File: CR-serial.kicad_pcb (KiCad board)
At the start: 2 copper layers, 55.6 x 43.9 mm, 26 parts, among them J1 USB, J2 GPIO, J3 UART0, J4 UART1, J5 UART2, J6 UART3_HV, J7 RS232_0, J8 RS232_1, U1 CP2108-xxx-xM, U2 MAX232

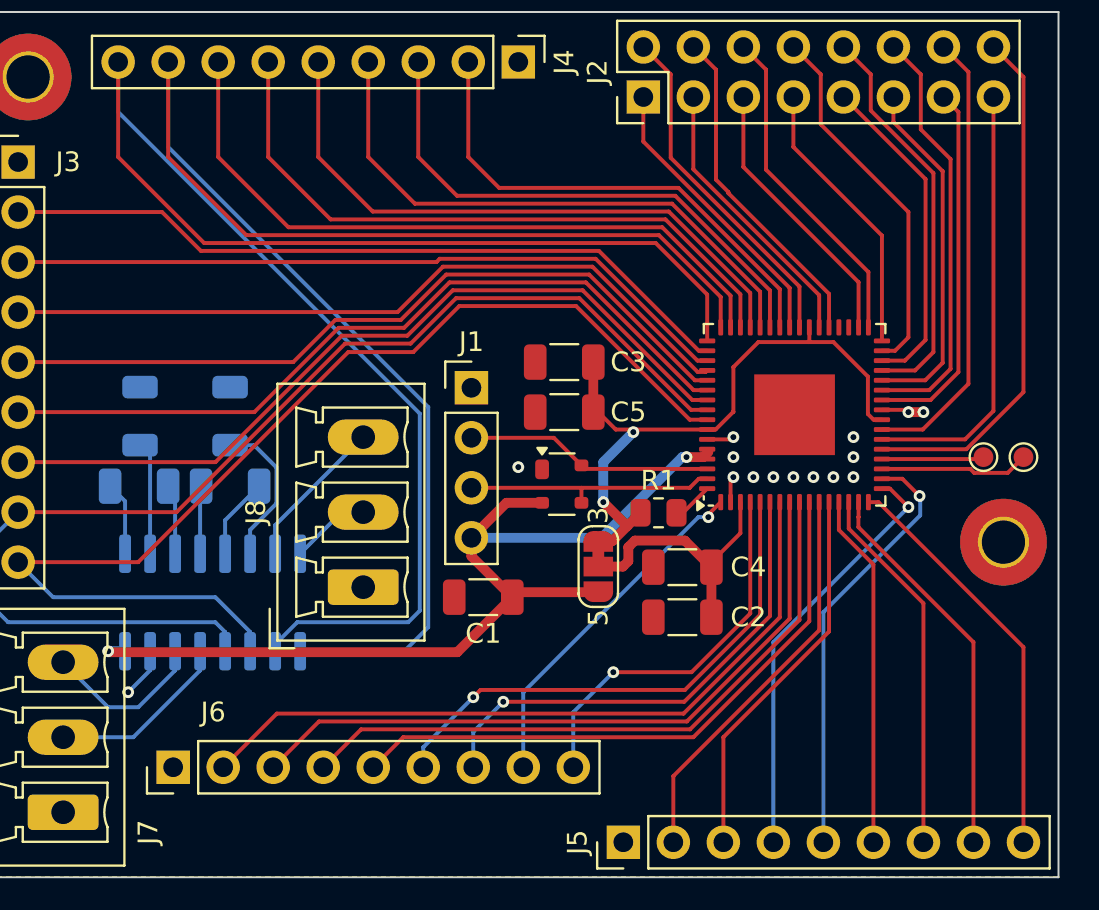
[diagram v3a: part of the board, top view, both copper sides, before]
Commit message: Add silkscreen markings
`--patience` is recommended for viewing
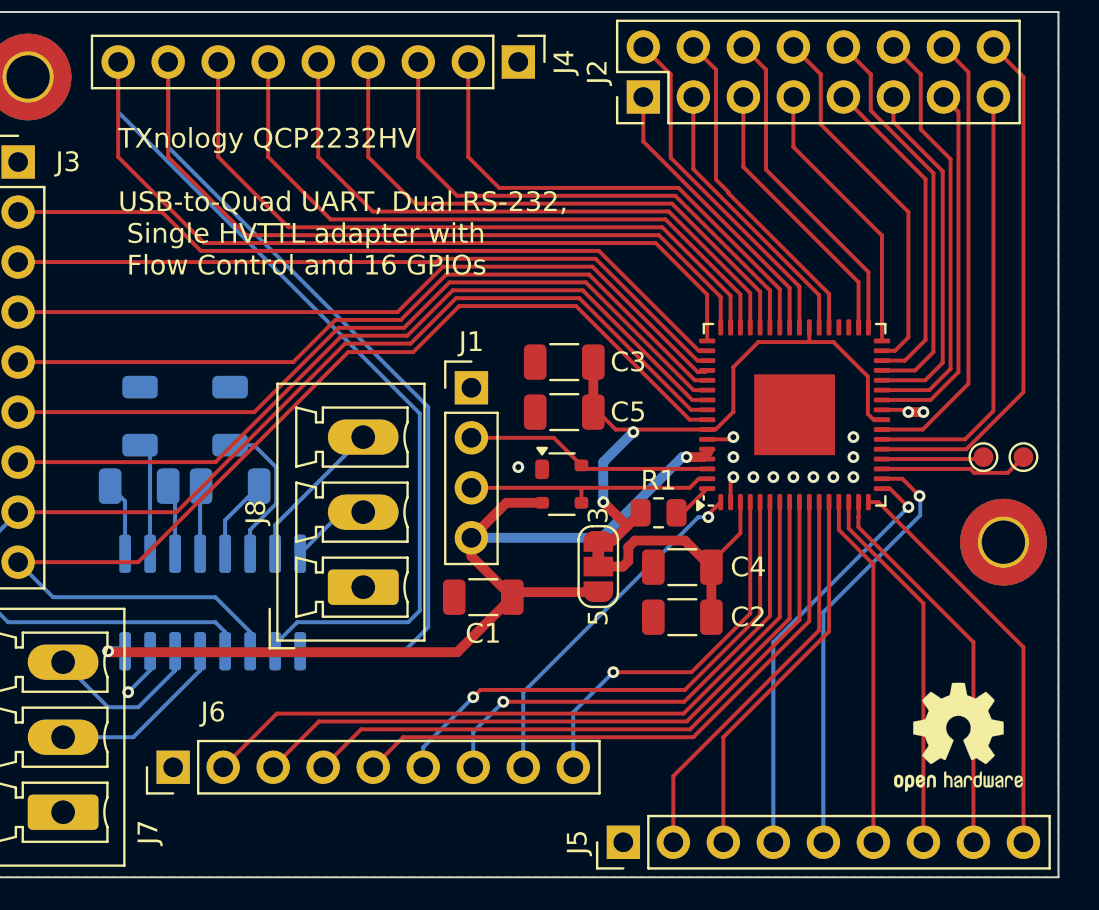
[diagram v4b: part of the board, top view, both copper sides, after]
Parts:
- added G***: QCP2232HV, LOGO, B.Cu at (205.5, 132.6)
- added REF**: OSHW-Logo2_7.3x6mm_SilkScreen, Symbol:OSHW-Logo2_7.3x6mm_SilkScreen, F.Cu at (208.3, 133.3)
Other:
- board text added: "S/N:"
- board text added: "TXnology QCP2232HV USB-to-Quad UART, Dual RS-232, Single HVTTL adapter with Flow Control and 16 GPIOs"

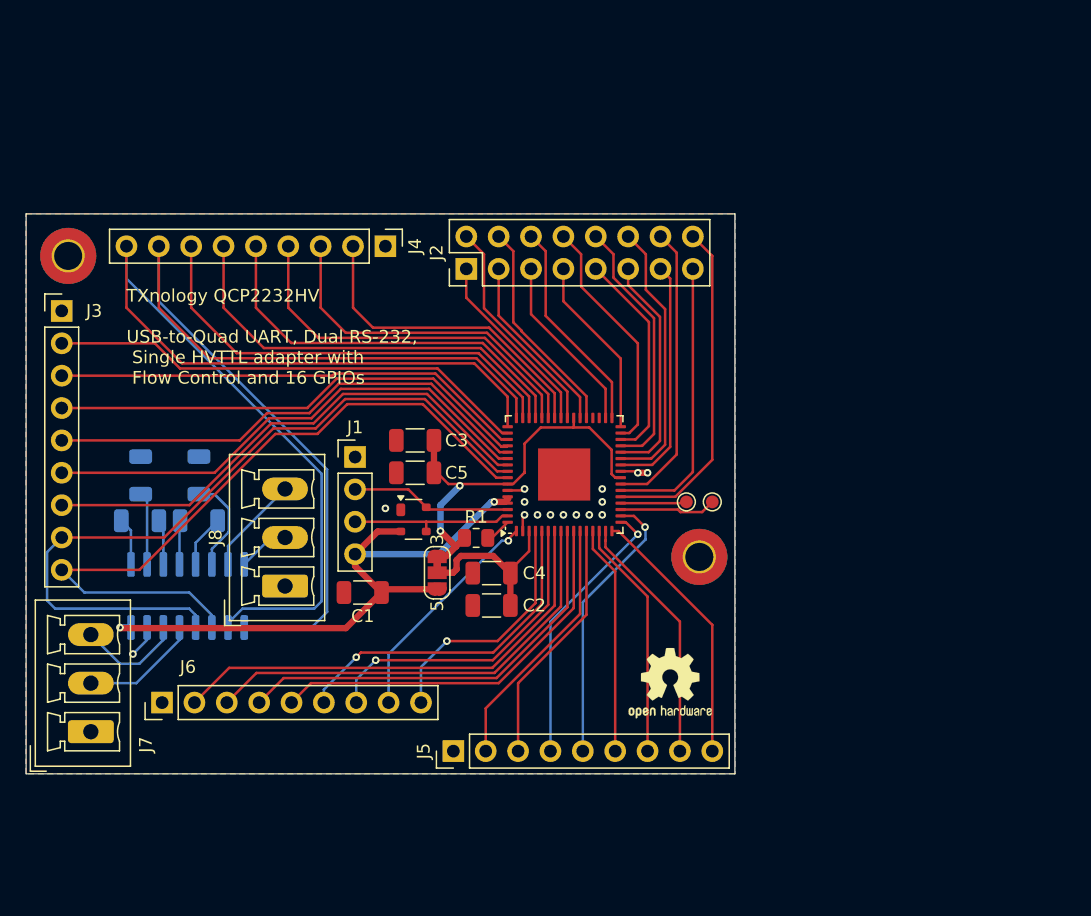
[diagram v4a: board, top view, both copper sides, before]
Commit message: New board
* 4 layers: internal VDD, GND plane
* connectors on board edge
* MAX232 on top
* product name on bottom
* lots of (nested) groups
* and of course, the schematic changes
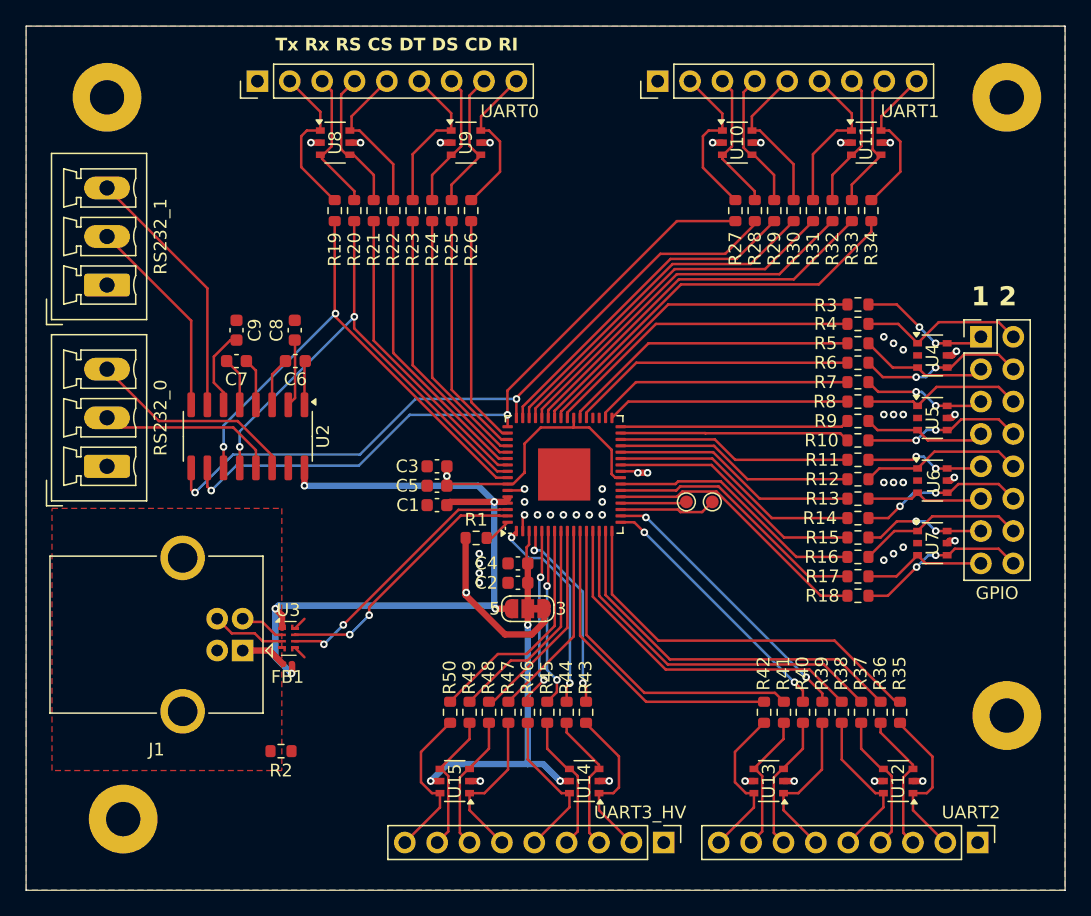
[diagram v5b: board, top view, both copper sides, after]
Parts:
- removed D1: SP0503BAHT, Package_TO_SOT_SMD:SOT-143
- removed REF**: OSHW-Logo2_7.3x6mm_SilkScreen, Symbol:OSHW-Logo2_7.3x6mm_SilkScreen
- added FB1: BLM18PG181SN1D, Inductor_SMD:L_0201_0603Metric, F.Cu at (178.2, 131.8)
- added H3: M2.5, MountingHole:MountingHole_2.7mm_M2.5_Pad, F.Cu at (234.7, 87.4)
- added H4: M2.5, MountingHole:MountingHole_2.7mm_M2.5_Pad, F.Cu at (234.7, 135.9)
- added R10: 100R, Resistor_SMD:R_0603_1608Metric, F.Cu at (223.0, 114.3)
- added R11: 100R, Resistor_SMD:R_0603_1608Metric, F.Cu at (223.0, 115.8)
- added R12: 100R, Resistor_SMD:R_0603_1608Metric, F.Cu at (223.0, 117.3)
- added R13: 100R, Resistor_SMD:R_0603_1608Metric, F.Cu at (223.0, 118.9)
- added R14: 100R, Resistor_SMD:R_0603_1608Metric, F.Cu at (223.0, 120.4)
- added R15: 100R, Resistor_SMD:R_0603_1608Metric, F.Cu at (223.0, 121.9)
- added R16: 100R, Resistor_SMD:R_0603_1608Metric, F.Cu at (223.0, 123.4)
- added R17: 100R, Resistor_SMD:R_0603_1608Metric, F.Cu at (223.0, 125.0)
- added R18: 100R, Resistor_SMD:R_0603_1608Metric, F.Cu at (223.0, 126.5)
- added R19: 100R, Resistor_SMD:R_0603_1608Metric, F.Cu at (182.0, 96.3)
- added R2: 0R, Resistor_SMD:R_0603_1608Metric, F.Cu at (177.7, 138.7)
- added R20: 100R, Resistor_SMD:R_0603_1608Metric, F.Cu at (183.5, 96.3)
- added R21: 100R, Resistor_SMD:R_0603_1608Metric, F.Cu at (185.0, 96.3)
- added R22: 100R, Resistor_SMD:R_0603_1608Metric, F.Cu at (186.5, 96.3)
- added R23: 100R, Resistor_SMD:R_0603_1608Metric, F.Cu at (188.1, 96.3)
- added R24: 100R, Resistor_SMD:R_0603_1608Metric, F.Cu at (189.6, 96.3)
- added R25: 100R, Resistor_SMD:R_0603_1608Metric, F.Cu at (191.1, 96.3)
- added R26: 100R, Resistor_SMD:R_0603_1608Metric, F.Cu at (192.7, 96.3)
- added R27: 100R, Resistor_SMD:R_0603_1608Metric, F.Cu at (213.4, 96.3)
- added R28: 100R, Resistor_SMD:R_0603_1608Metric, F.Cu at (214.9, 96.3)
- added R29: 100R, Resistor_SMD:R_0603_1608Metric, F.Cu at (216.4, 96.3)
- added R3: 100R, Resistor_SMD:R_0603_1608Metric, F.Cu at (223.0, 103.6)
- added R30: 100R, Resistor_SMD:R_0603_1608Metric, F.Cu at (218.0, 96.3)
- added R31: 100R, Resistor_SMD:R_0603_1608Metric, F.Cu at (219.5, 96.3)
- added R32: 100R, Resistor_SMD:R_0603_1608Metric, F.Cu at (221.0, 96.3)
- added R33: 100R, Resistor_SMD:R_0603_1608Metric, F.Cu at (222.5, 96.3)
- added R34: 100R, Resistor_SMD:R_0603_1608Metric, F.Cu at (224.1, 96.3)
- added R35: 100R, Resistor_SMD:R_0603_1608Metric, F.Cu at (226.3, 135.6)
- added R36: 100R, Resistor_SMD:R_0603_1608Metric, F.Cu at (224.8, 135.6)
- added R37: 100R, Resistor_SMD:R_0603_1608Metric, F.Cu at (223.3, 135.6)
- added R38: 100R, Resistor_SMD:R_0603_1608Metric, F.Cu at (221.7, 135.6)
- added R39: 100R, Resistor_SMD:R_0603_1608Metric, F.Cu at (220.2, 135.6)
- added R4: 100R, Resistor_SMD:R_0603_1608Metric, F.Cu at (223.0, 105.2)
- added R40: 100R, Resistor_SMD:R_0603_1608Metric, F.Cu at (218.7, 135.6)
- added R41: 100R, Resistor_SMD:R_0603_1608Metric, F.Cu at (217.2, 135.6)
- added R42: 100R, Resistor_SMD:R_0603_1608Metric, F.Cu at (215.6, 135.6)
- added R43: 100R, Resistor_SMD:R_0603_1608Metric, F.Cu at (201.7, 135.6)
- added R44: 100R, Resistor_SMD:R_0603_1608Metric, F.Cu at (200.2, 135.6)
- added R45: 100R, Resistor_SMD:R_0603_1608Metric, F.Cu at (198.6, 135.6)
- added R46: 100R, Resistor_SMD:R_0603_1608Metric, F.Cu at (197.1, 135.6)
- added R47: 100R, Resistor_SMD:R_0603_1608Metric, F.Cu at (195.6, 135.6)
- added R48: 100R, Resistor_SMD:R_0603_1608Metric, F.Cu at (194.1, 135.6)
- added R49: 100R, Resistor_SMD:R_0603_1608Metric, F.Cu at (192.5, 135.6)
- added R5: 100R, Resistor_SMD:R_0603_1608Metric, F.Cu at (223.0, 106.7)
- added R50: 100R, Resistor_SMD:R_0603_1608Metric, F.Cu at (191.0, 135.6)
- added R6: 100R, Resistor_SMD:R_0603_1608Metric, F.Cu at (223.0, 108.2)
- added R7: 100R, Resistor_SMD:R_0603_1608Metric, F.Cu at (223.0, 109.7)
- added R8: 100R, Resistor_SMD:R_0603_1608Metric, F.Cu at (223.0, 111.3)
- added R9: 100R, Resistor_SMD:R_0603_1608Metric, F.Cu at (223.0, 112.8)
- added U10: TVS4201MR6, Package_SO:TSOP-6_1.65x3.05mm_P0.95mm, F.Cu at (213.5, 90.9)
- added U11: TVS4201MR6, Package_SO:TSOP-6_1.65x3.05mm_P0.95mm, F.Cu at (223.7, 90.9)
- added U12: TVS4201MR6, Package_SO:TSOP-6_1.65x3.05mm_P0.95mm, F.Cu at (226.2, 141.0)
- added U13: TVS4201MR6, Package_SO:TSOP-6_1.65x3.05mm_P0.95mm, F.Cu at (216.0, 141.0)
- added U14: TVS4201MR6, Package_SO:TSOP-6_1.65x3.05mm_P0.95mm, F.Cu at (201.5, 141.0)
- added U15: TVS4201MR6, Package_SO:TSOP-6_1.65x3.05mm_P0.95mm, F.Cu at (191.4, 141.0)
- added U3: ECMF02-4CMX8, QCP_parts:ST_UQFN-8L_1.15x2.45mm_P0.5mm, F.Cu at (178.3, 129.8)
- added U4: TVS4201MR6, Package_SO:TSOP-6_1.65x3.05mm_P0.95mm, F.Cu at (228.9, 107.6)
- added U5: TVS4201MR6, Package_SO:TSOP-6_1.65x3.05mm_P0.95mm, F.Cu at (228.9, 112.5)
- added U6: TVS4201MR6, Package_SO:TSOP-6_1.65x3.05mm_P0.95mm, F.Cu at (228.9, 117.5)
- added U7: TVS4201MR6, Package_SO:TSOP-6_1.65x3.05mm_P0.95mm, F.Cu at (228.9, 122.4)
- added U8: TVS4201MR6, Package_SO:TSOP-6_1.65x3.05mm_P0.95mm, F.Cu at (182.0, 90.9)
- added U9: TVS4201MR6, Package_SO:TSOP-6_1.65x3.05mm_P0.95mm, F.Cu at (192.3, 90.9)
- C1, C2, C3: value 1u -> 10u; footprint Capacitor_SMD:C_1206_3216Metric -> Capacitor_SMD:C_0603_1608Metric
- C4, C5: footprint Capacitor_SMD:C_1206_3216Metric -> Capacitor_SMD:C_0603_1608Metric
- C6, C7, C8, C9: footprint Capacitor_SMD:C_1206_3216Metric -> Capacitor_SMD:C_0603_1608Metric; moved to F.Cu
- H1, H2: value M2 -> M2.5; footprint MountingHole:MountingHole_2.2mm_M2_Pad_TopBottom -> MountingHole:MountingHole_2.7mm_M2.5_Pad
- J1: value USB -> USB_B; footprint Connector_PinHeader_2.54mm:PinHeader_1x04_P2.54mm_Vertical -> Connector_USB:USB_B_OST_USB-B1HSxx_Horizontal
- R1: footprint Resistor_SMD:R_0805_2012Metric -> Resistor_SMD:R_0603_1608Metric
- U2: moved to F.Cu
- moved H2 49.7 mm to (165.4, 144.0)
- moved J5 41.8 mm to (232.4, 145.9), turned to -90 degrees
- moved J6 40.9 mm to (207.8, 145.9), turned to -90 degrees
- moved J2 40.7 mm to (232.7, 106.2), turned to 0 degrees
- moved J8 27.4 mm to (164.1, 102.1)
- moved J4 25.0 mm to (207.3, 86.1), turned to 90 degrees
- moved J3 23.7 mm to (175.9, 86.1), turned to 90 degrees
- moved J7 20.9 mm to (164.1, 116.3)
- moved G*** 19.3 mm to (187.5, 139.4)
- moved J1 17.6 mm to (174.7, 130.8), turned to 180 degrees
- moved C6 17.5 mm to (178.9, 108.1), turned to 180 degrees
- moved C8 16.6 mm to (178.8, 105.7)
- moved U2 13.4 mm to (175.1, 114.0)
- moved C7 12.9 mm to (174.2, 108.1), turned to 180 degrees
- moved H1 12.8 mm to (164.1, 87.4)
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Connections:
- J1 pad 1: GND -> Net-(J1-VBUS)
- J1 pad 2: Net-(J1-Pin_2) -> Net-(J1-D-)
- J1 pad 3: Net-(J1-Pin_3) -> Net-(J1-D+)
- J1 pad 4: VBUS -> GND
- J2 pad 1: Net-(J2-Pin_1) -> /UART/J2P1
- J2 pad 10: Net-(J2-Pin_10) -> /UART/J2Pa
- J2 pad 11: Net-(J2-Pin_11) -> /UART/J2Pb
- J2 pad 12: Net-(J2-Pin_12) -> /UART/J2Pc
- J2 pad 13: Net-(J2-Pin_13) -> /UART/J2Pd
- J2 pad 14: Net-(J2-Pin_14) -> /UART/J2Pe
- J2 pad 15: Net-(J2-Pin_15) -> /UART/J2Pf
- J2 pad 16: Net-(J2-Pin_16) -> /UART/J2Pg
- J2 pad 2: Net-(J2-Pin_2) -> /UART/J2P2
- J2 pad 3: Net-(J2-Pin_3) -> /UART/J2P3
- J2 pad 4: Net-(J2-Pin_4) -> /UART/J2P4
- J2 pad 5: Net-(J2-Pin_5) -> /UART/J2P5
- J2 pad 6: Net-(J2-Pin_6) -> /UART/J2P6
- J2 pad 7: Net-(J2-Pin_7) -> /UART/J2P7
- J2 pad 8: Net-(J2-Pin_8) -> /UART/J2P8
- J2 pad 9: Net-(J2-Pin_9) -> /UART/J2P9
- J3 pad 2: Net-(J3-Pin_2) -> /UART/J3P2
- J3 pad 3: Net-(J3-Pin_3) -> /UART/J3P3
- J3 pad 4: Net-(J3-Pin_4) -> /UART/J3P4
- J3 pad 5: Net-(J3-Pin_5) -> /UART/J3P5
- J3 pad 6: Net-(J3-Pin_6) -> /UART/J3P6
- J3 pad 7: Net-(J3-Pin_7) -> /UART/J3P7
- J3 pad 8: /RX0 -> /UART/J3P8
- J3 pad 9: /TX0 -> /UART/J3P9
- J4 pad 2: Net-(J4-Pin_2) -> /UART/J4P2
- J4 pad 3: Net-(J4-Pin_3) -> /UART/J4P3
- J4 pad 4: Net-(J4-Pin_4) -> /UART/J4P4
- J4 pad 5: Net-(J4-Pin_5) -> /UART/J4P5
- J4 pad 6: Net-(J4-Pin_6) -> /UART/J4P6
- J4 pad 7: Net-(J4-Pin_7) -> /UART/J4P7
- J4 pad 8: /RX1 -> /UART/J4P8
- J4 pad 9: /TX1 -> /UART/J4P9
- J5 pad 2: Net-(J5-Pin_2) -> /UART/J5P2
- J5 pad 3: Net-(J5-Pin_3) -> /UART/J5P3
- J5 pad 4: Net-(J5-Pin_4) -> /UART/J5P4
- J5 pad 5: Net-(J5-Pin_5) -> /UART/J5P5
- J5 pad 6: Net-(J5-Pin_6) -> /UART/J5P6
- J5 pad 7: Net-(J5-Pin_7) -> /UART/J5P7
- J5 pad 8: Net-(J5-Pin_8) -> /UART/J5P8
- J5 pad 9: Net-(J5-Pin_9) -> /UART/J5P9
- J6 pad 2: Net-(J6-Pin_2) -> /UART/J6P2
- J6 pad 3: Net-(J6-Pin_3) -> /UART/J6P3
- J6 pad 4: Net-(J6-Pin_4) -> /UART/J6P4
- J6 pad 5: Net-(J6-Pin_5) -> /UART/J6P5
- J6 pad 6: Net-(J6-Pin_6) -> /UART/J6P6
- J6 pad 7: Net-(J6-Pin_7) -> /UART/J6P7
- J6 pad 8: Net-(J6-Pin_8) -> /UART/J6P8
- J6 pad 9: Net-(J6-Pin_9) -> /UART/J6P9
- U1 pad 1: Net-(J6-Pin_8) -> RX3
- U1 pad 10: Net-(J6-Pin_5) -> DTR3
- U1 pad 11: Net-(J5-Pin_2) -> RI2
- U1 pad 12: Net-(J5-Pin_3) -> DCD2
- U1 pad 13: Net-(J5-Pin_6) -> CTS2
- U1 pad 14: Net-(J5-Pin_7) -> RTS2
- U1 pad 15: Net-(J5-Pin_8) -> RX2
- U1 pad 16: Net-(J5-Pin_9) -> TX2
- U1 pad 17: Net-(J5-Pin_4) -> DSR2
- U1 pad 18: Net-(J5-Pin_5) -> DTR2
- U1 pad 21: Net-(J2-Pin_16) -> GPIO15
- U1 pad 22: Net-(J2-Pin_15) -> GPIO14
- U1 pad 23: Net-(J2-Pin_14) -> GPIO13
- U1 pad 26: Net-(J2-Pin_13) -> GPIO12
- U1 pad 27: Net-(J2-Pin_12) -> GPIO11
- U1 pad 28: Net-(J2-Pin_11) -> GPIO10
- U1 pad 29: Net-(J2-Pin_10) -> GPIO9
- U1 pad 30: Net-(J2-Pin_9) -> GPIO8
- U1 pad 31: Net-(J2-Pin_8) -> GPIO7
- U1 pad 32: Net-(J2-Pin_7) -> GPIO6
- U1 pad 33: Net-(J2-Pin_6) -> GPIO5
- U1 pad 34: Net-(J2-Pin_5) -> GPIO4
- U1 pad 37: Net-(J2-Pin_4) -> GPIO3
- U1 pad 38: Net-(J2-Pin_3) -> GPIO2
- U1 pad 4: Net-(J6-Pin_9) -> TX3
- U1 pad 40: Net-(J2-Pin_2) -> GPIO1
- U1 pad 41: Net-(J2-Pin_1) -> GPIO0
- U1 pad 42: Net-(J4-Pin_2) -> RI1
- U1 pad 43: Net-(J4-Pin_3) -> DCD1
- U1 pad 44: Net-(J4-Pin_4) -> DSR1
- U1 pad 45: Net-(J4-Pin_5) -> DTR1
- U1 pad 46: Net-(J4-Pin_6) -> CTS1
- U1 pad 47: Net-(J4-Pin_7) -> RTS1
- U1 pad 48: /RX1 -> RX1
- U1 pad 49: /TX1 -> TX1
- U1 pad 5: Net-(J6-Pin_6) -> CTS3
- U1 pad 50: Net-(J3-Pin_2) -> RI0
- U1 pad 51: Net-(J3-Pin_3) -> DCD0
- U1 pad 52: Net-(J3-Pin_4) -> DSR0
- U1 pad 53: Net-(J3-Pin_5) -> DTR0
- U1 pad 54: Net-(J3-Pin_6) -> CTS0
- U1 pad 55: Net-(J3-Pin_7) -> RTS0
- U1 pad 56: /RX0 -> RX0
- U1 pad 57: /TX0 -> TX0
- U1 pad 6: Net-(J6-Pin_7) -> RTS3
- U1 pad 62: Net-(J1-Pin_2) -> /D+
- U1 pad 63: Net-(J1-Pin_3) -> /D-
- U1 pad 7: Net-(J6-Pin_2) -> RI3
- U1 pad 8: Net-(J6-Pin_3) -> DCD3
- U1 pad 9: Net-(J6-Pin_4) -> DSR3
- U2 pad 10: /TX1 -> TX1
- U2 pad 11: /TX0 -> TX0
- U2 pad 12: /RX0 -> RX0
- U2 pad 9: /RX1 -> RX1
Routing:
- net /TX1: track 82.6 -> 0.00 mm
- net /RX1: track 78.6 -> 0.00 mm
- net /RX0: track 60.4 -> 0.00 mm
- net /TX0: track 57.0 -> 0.00 mm
- net RX1: track 0.00 -> 56.8 mm, vias 0 -> 2
- net TX1: track 0.00 -> 53.9 mm, vias 0 -> 2
- net TX0: track 0.00 -> 42.0 mm, vias 0 -> 2
- net Net-(J3-Pin_7): track 40.9 -> 0.00 mm
- net RX0: track 0.00 -> 40.7 mm, vias 0 -> 2
- net Net-(J3-Pin_6): track 40.0 -> 0.00 mm
- net Net-(J3-Pin_5): track 39.1 -> 0.00 mm
- net Net-(J3-Pin_4): track 38.2 -> 0.00 mm
- net Net-(J3-Pin_2): track 37.9 -> 0.00 mm
- net Net-(J6-Pin_2): track 37.3 -> 0.00 mm
- net Net-(J3-Pin_3): track 37.2 -> 0.00 mm
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- added copper zone on In2.Cu, net GND
- added copper zone on F.Cu, net Net-(J1-Shield)
- added copper zone on In1.Cu, net VDD
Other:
- board size 55.6 x 43.9 mm -> 81.5 x 67.8 mm
- copper layers 2 -> 4
- board text added: "1 2"
- board text added: "Tx Rx RS CS DT DS CD RI"

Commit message: More silkscreen work
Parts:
- moved G*** 3.97 mm to (190.0, 136.4)
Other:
- board text added: "0 1"
- board text added: "Alternate functions"
- board text added: "RI CD DS DT CS RS Rx Tx"
- board text added: "Tx Rx G"
- board text removed: "1 2"
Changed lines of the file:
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@@
 		)
 		(property "Value" "Vsel"
-			(at 0 1.9 0)
-			(layer "F.Fab")
+			(at 0 -2.032 0)
+			(layer "F.SilkS")
 			(effects
 				(font
@@
 	(footprint "LOGO"
 		(layer "B.Cu")
-		(at 187.452 139.446 180)
+		(at 189.992 136.398 180)
 		(property "Reference" "G***"
 			(at 0 0 0)
@@
 	)
 	(gr_rect
-		(start 173.482 139.192)
-		(end 180.086 142.494)
+		(start 176.022 136.144)
+		(end 182.626 139.446)
 		(stroke
 			(width 0.1)
@@
 	)
 	(gr_text "S/N:"
-		(at 180.34 137.414 0)
+		(at 182.88 134.366 0)
 		(layer "B.SilkS")
 		(effects
@@
 		)
 	)
+	(gr_text "Alternate functions"
+		(at 225.298 121.539 270)
+		(layer "B.SilkS")
+		(effects
+			(font
+				(size 1 1)
+				(thickness 0.1)
+			)
+			(justify bottom mirror)
+		)
+	)
+	(gr_text "Tx   Rx   G"
+		(at 158.242 98.044 270)
+		(layer "F.SilkS")
+		(effects
+			(font
+				(size 1 1)
+				(thickness 0.2)
+				(bold yes)
+			)
+			(justify bottom)
+		)
+	)
 	(gr_text "Tx Rx RS CS DT DS CD RI"
 		(at 177.292 83.82 0)
@@
 		)
 	)
-	(gr_text "1 2"
+	(gr_text "RI CD DS DT CS RS Rx Tx"
+		(at 211.074 147.828 0)
+		(layer "F.SilkS")
+		(effects
+			(font
+				(size 1 1)
+				(thickness 0.15)
+				(bold yes)
+			)
+			(justify left top)
+		)
+	)
+	(gr_text "Tx Rx RS CS DT DS CD RI"
+		(at 208.568 83.82 0)
+		(layer "F.SilkS")
+		(effects
+			(font
+				(size 1 1)
+				(thickness 0.15)
+				(bold yes)
+			)
+			(justify left bottom)
+		)
+	)
+	(gr_text "0 1"
 		(at 231.902 103.886 0)
 		(layer "F.SilkS")
@@
 		)
 	)
+	(gr_text "RI CD DS DT CS RS Rx Tx"
+		(at 186.436 147.828 0)
+		(layer "F.SilkS")
+		(effects
+			(font
+				(size 1 1)
+				(thickness 0.15)
+				(bold yes)
+			)
+			(justify left top)
+		)
+	)
+	(gr_text "Tx   Rx   G"
+		(at 158.242 112.522 270)
+		(layer "F.SilkS")
+		(effects
+			(font
+				(size 1 1)
+				(thickness 0.2)
+				(bold yes)
+			)
+			(justify bottom)
+		)
+	)
+	(gr_text_box "		Flow Ctl	RS232	Vsel\nUART0	Y			Y\nUART1	Y			Y\nUART2	Y\nUART3	Y					Y"
+		(start 192.405 102.616)
+		(end 224.409 111.506)
+		(layer "B.SilkS")
+		(effects
+			(font
+				(size 1 1)
+				(thickness 0.1)
+			)
+			(justify left top mirror)
+		)
+		(border yes)
+		(stroke
+			(width 0.1)
+			(type solid)
+		)
+	)
+	(gr_text_box "GPIO #	UART #	Tx LED	Rx LED	Tx/~Rx	CLK\n0		0		*\n1		0				*\n2		0						*\n3		0								*\n4		1		*\n5		1				*\n6		1						*\n7		1								*\n8-11	2				  - {dblquote} -\n12-15	3				  - {dblquote} -"
+		(start 179.959 111.887)
+		(end 224.409 131.191)
+		(layer "B.SilkS")
+		(effects
+			(font
+				(size 1 1)
+				(thickness 0.1)
+			)
+			(justify left top mirror)
+		)
+		(border yes)
+		(stroke
+			(width 0.1)
+			(type solid)
+		)
+	)

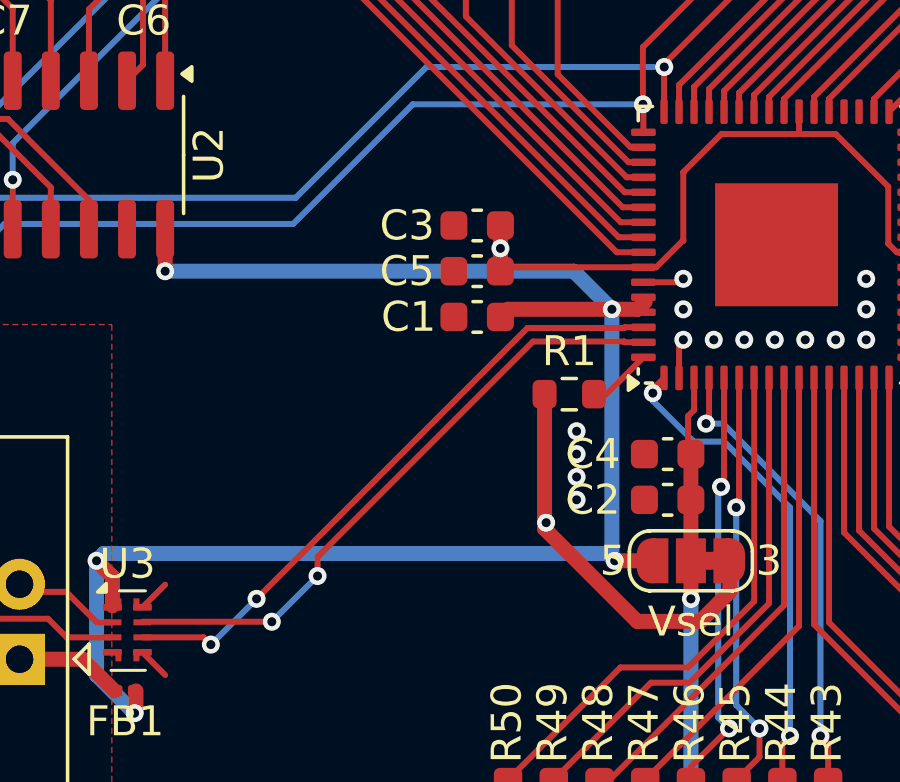
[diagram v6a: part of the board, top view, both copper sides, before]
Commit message: Re-add OSHW logo, add GH URL, move caps
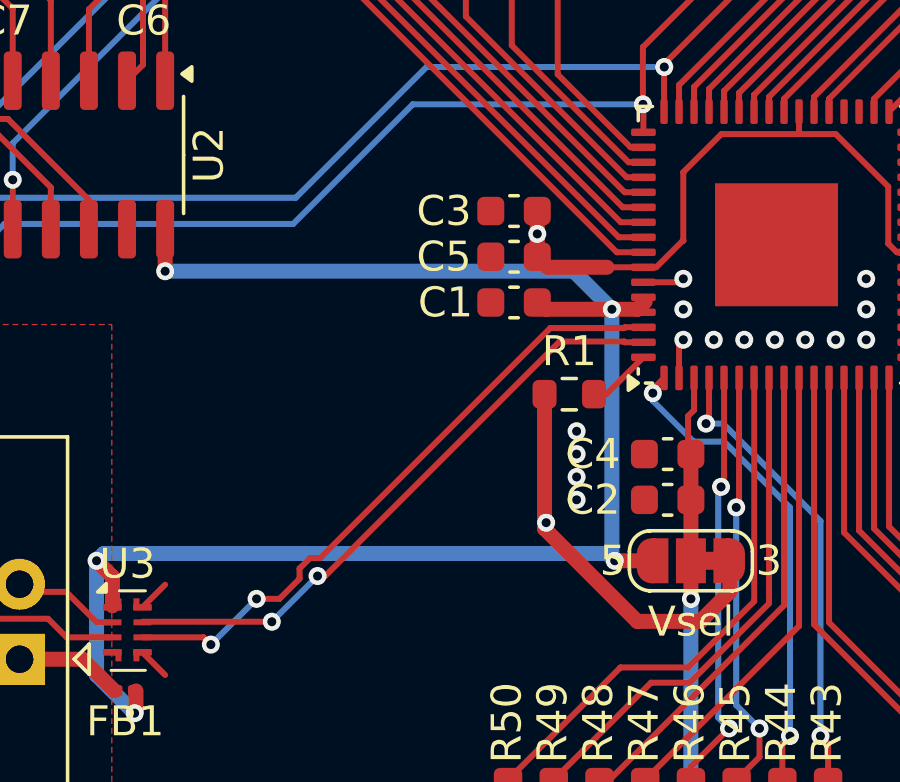
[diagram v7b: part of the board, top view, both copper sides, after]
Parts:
- added SYM1: Logo_Open_Hardware_Small, Symbol:OSHW-Logo2_7.3x6mm_SilkScreen, B.Cu at (221.0, 137.7)
- moved C1 1.32 mm to (191.2, 118.9)
- moved C5 1.32 mm to (191.2, 117.4)
- moved C3 1.32 mm to (191.2, 115.9)
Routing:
- net VBUS: track 57.1 -> 55.8 mm
- net VDD: track 42.6 -> 41.5 mm
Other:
- board text added: "https://github.com/bence98/qcp2232"
